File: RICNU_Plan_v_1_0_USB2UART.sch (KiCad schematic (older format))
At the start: 5 parts, among them U4 FT232RL

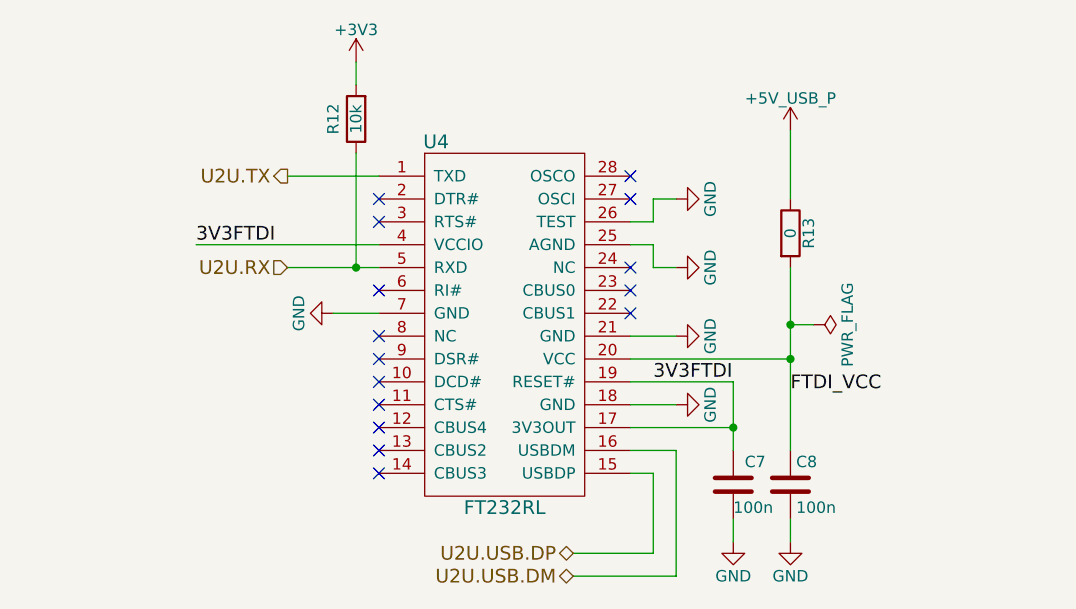
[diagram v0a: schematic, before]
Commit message: Added connections to monitor power, changed CANSTB MCU pin, moved LED pins around
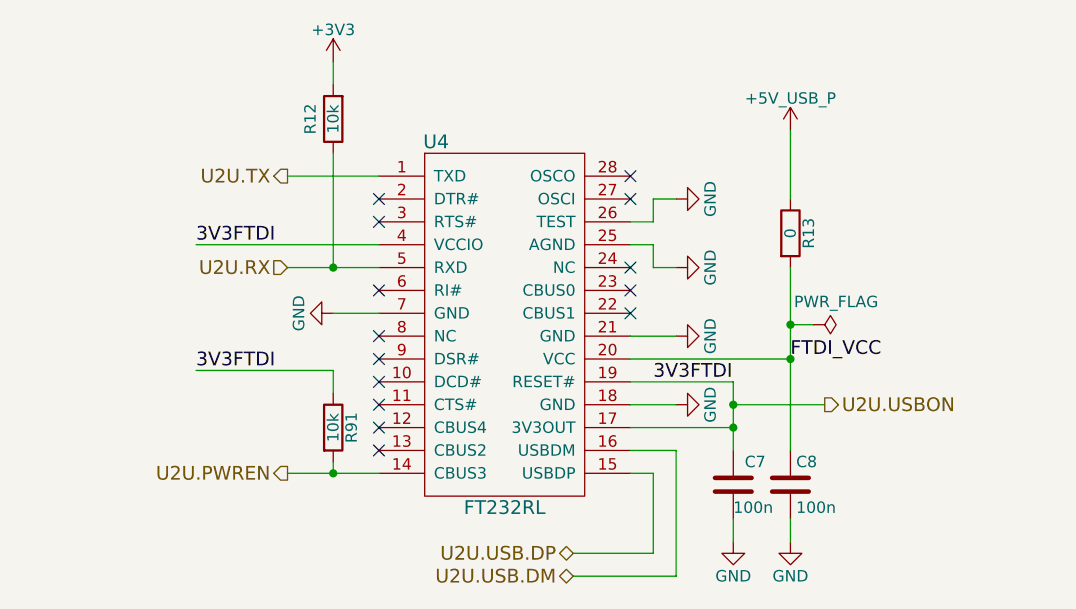
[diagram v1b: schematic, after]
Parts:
- added R91: 10k, Resistors_SMD:R_0402_NoSilk, symbol R
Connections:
- net U2U.PWREN: now reaches U4.14 (CBUS3)
- net U2U.PWREN: now also R91.2
- net 3V3FTDI renamed U2U.USBON
- net U2U.USBON: now also R91.1
- no-connect marks 15 -> 14
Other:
- moved on the sheet: R12
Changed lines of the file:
@@
 L R R12
 U 1 1 59FB130B
-P 5250 3100
-F 0 "R12" V 5350 3100 50  0000 C CNN
-F 1 "10k" V 5250 3100 50  0000 C CNN
-F 2 "Resistors_SMD:R_0402_NoSilk" V 5180 3100 50  0001 C CNN
-F 3 "" H 5250 3100 50  0001 C CNN
-	1    5250 3100
+P 5150 3100
+F 0 "R12" V 5250 3100 50  0000 C CNN
+F 1 "10k" V 5150 3100 50  0000 C CNN
+F 2 "Resistors_SMD:R_0402_NoSilk" V 5080 3100 50  0001 C CNN
+F 3 "" H 5150 3100 50  0001 C CNN
+	1    5150 3100
 	-1   0    0    1
 $EndComp
@@
 NoConn ~ 5350 4450
 NoConn ~ 5350 4550
-NoConn ~ 5350 4650
 NoConn ~ 6450 3850
 NoConn ~ 6450 3950
@@
 L +3V3 #PWR025
 U 1 1 59FB95AB
-P 5250 2850
-F 0 "#PWR025" H 5250 2700 50  0001 C CNN
-F 1 "+3V3" H 5250 2990 50  0000 C CNN
-F 2 "" H 5250 2850 50  0001 C CNN
-F 3 "" H 5250 2850 50  0001 C CNN
-	1    5250 2850
+P 5150 2850
+F 0 "#PWR025" H 5150 2700 50  0001 C CNN
+F 1 "+3V3" H 5150 2990 50  0000 C CNN
+F 2 "" H 5150 2850 50  0001 C CNN
+F 3 "" H 5150 2850 50  0001 C CNN
+	1    5150 2850
 	1    0    0    -1
 $EndComp
@@
 	6450 4650 6550 4650
 Wire Wire Line
-	6450 4450 6900 4450
-Wire Wire Line
-	6450 4150 7150 4150
+	6900 4450 6450 4450
+Wire Wire Line
+	7150 4150 6450 4150
 Wire Wire Line
 	7150 3750 7150 4550
@@
 	4950 3750 5350 3750
 Wire Wire Line
-	5250 3750 5250 3250
-Wire Wire Line
-	5250 2850 5250 2950
-Connection ~ 5250 3750
+	5150 3750 5150 3250
+Wire Wire Line
+	5150 2850 5150 2950
+Connection ~ 5150 3750
 Wire Wire Line
 	4950 3350 5350 3350
@@
 P 7250 4000
 F 0 "#FLG032" H 7250 4075 50  0001 C CNN
-F 1 "PWR_FLAG" H 7250 4150 50  0000 C CNN
+F 1 "PWR_FLAG" V 7150 4100 50  0000 C CNN
 F 2 "" H 7250 4000 50  0001 C CNN
 F 3 "" H 7250 4000 50  0001 C CNN
@@
 	7250 4000 7150 4000
 Connection ~ 7150 4000
-Text Label 7150 4300 0    60   ~ 0
+Text Label 7150 4150 0    60   ~ 0
 FTDI_VCC
+$Comp
+L R R91
+U 1 1 5A20B32A
+P 5150 4450
+F 0 "R91" V 5230 4450 50  0000 C CNN
+F 1 "10k" V 5150 4450 50  0000 C CNN
+F 2 "Resistors_SMD:R_0402_NoSilk" V 5080 4450 50  0001 C CNN
+F 3 "" H 5150 4450 50  0001 C CNN
+	1    5150 4450
+	1    0    0    -1
+$EndComp
+Wire Wire Line
+	4950 4650 5350 4650
+Wire Wire Line
+	5150 4650 5150 4600
+Wire Wire Line
+	5150 4200 5150 4300
+Connection ~ 5150 4650
+Text HLabel 4950 4650 0    60   Output ~ 0
+U2U.PWREN
+Text HLabel 7300 4350 2    60   Output ~ 0
+U2U.USBON
+Wire Wire Line
+	6900 4350 7300 4350
+Connection ~ 6900 4350
+Wire Wire Line
+	5150 4200 4550 4200
+Text Label 4550 4200 0    60   ~ 0
+3V3FTDI
 $EndSCHEMATC

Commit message: Various small changes like comment removal
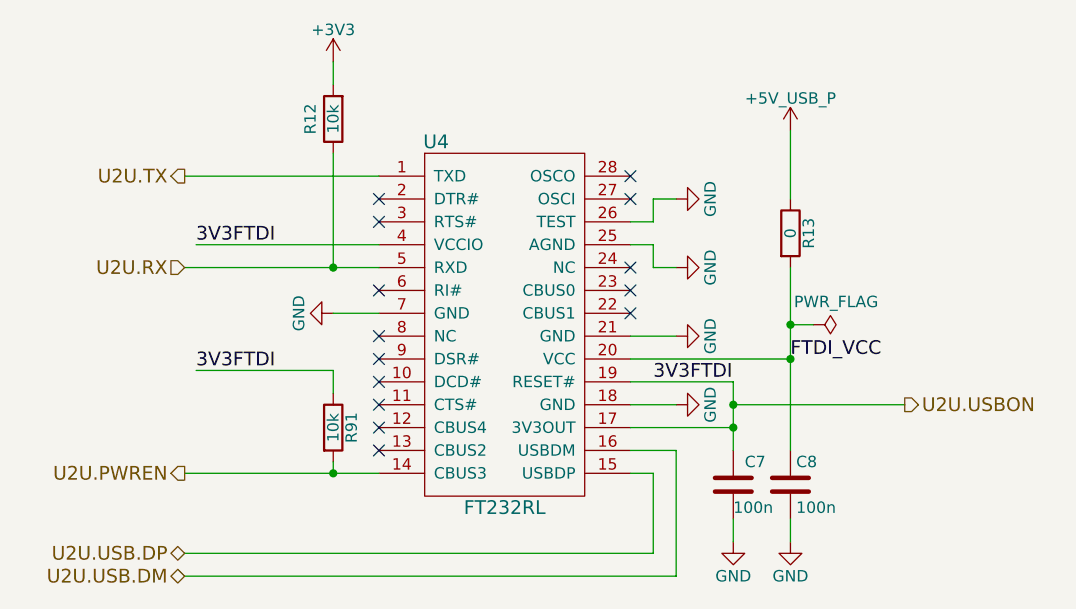
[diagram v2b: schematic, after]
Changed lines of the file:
@@
 	1    0    0    -1
 $EndComp
-Text HLabel 4950 3350 0    60   Output ~ 0
+Text HLabel 4500 3350 0    60   Output ~ 0
 U2U.TX
-Text HLabel 4950 3750 0    60   Input ~ 0
+Text HLabel 4500 3750 0    60   Input ~ 0
 U2U.RX
-Text HLabel 6200 5000 0    60   BiDi ~ 0
+Text HLabel 4500 5000 0    60   BiDi ~ 0
 U2U.USB.DP
-Text HLabel 6200 5100 0    60   BiDi ~ 0
+Text HLabel 4500 5100 0    60   BiDi ~ 0
 U2U.USB.DM
 $Comp
@@
 	7150 4150 6450 4150
 Wire Wire Line
-	7150 3750 7150 4550
+	7150 3750 7150 4000
+Wire Wire Line
+	7150 4000 7150 4150
+Wire Wire Line
+	7150 4150 7150 4550
 Wire Wire Line
 	7150 3150 7150 3450
 Connection ~ 7150 4150
 Wire Wire Line
-	4950 3750 5350 3750
+	4500 3750 5150 3750
+Wire Wire Line
+	5150 3750 5350 3750
 Wire Wire Line
 	5150 3750 5150 3250
@@
 Connection ~ 5150 3750
 Wire Wire Line
-	4950 3350 5350 3350
+	4500 3350 5350 3350
 Wire Wire Line
 	6900 4850 6900 4950
 Wire Wire Line
-	6900 4250 6900 4550
+	6900 4250 6900 4350
+Wire Wire Line
+	6900 4350 6900 4450
+Wire Wire Line
+	6900 4450 6900 4550
 Wire Wire Line
 	6450 4250 6900 4250
@@
 	6650 4050 6450 4050
 Wire Wire Line
-	6200 5000 6550 5000
+	4500 5000 6550 5000
 Wire Wire Line
 	6550 5000 6550 4650
 Wire Wire Line
-	6650 5100 6200 5100
+	6650 5100 4500 5100
 Wire Wire Line
 	5350 3950 5150 3950
@@
 $EndComp
 Wire Wire Line
-	4950 4650 5350 4650
+	4500 4650 5150 4650
+Wire Wire Line
+	5150 4650 5350 4650
 Wire Wire Line
 	5150 4650 5150 4600
@@
 	5150 4200 5150 4300
 Connection ~ 5150 4650
-Text HLabel 4950 4650 0    60   Output ~ 0
+Text HLabel 4500 4650 0    60   Output ~ 0
 U2U.PWREN
-Text HLabel 7300 4350 2    60   Output ~ 0
+Text HLabel 7650 4350 2    60   Output ~ 0
 U2U.USBON
 Wire Wire Line
-	6900 4350 7300 4350
+	6900 4350 7650 4350
 Connection ~ 6900 4350
 Wire Wire Line

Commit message: Deleting PDFs
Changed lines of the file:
@@
 	7150 4150 6450 4150
 Wire Wire Line
-	7150 3750 7150 4000
-Wire Wire Line
-	7150 4000 7150 4150
-Wire Wire Line
-	7150 4150 7150 4550
+	7150 3750 7150 4550
 Wire Wire Line
 	7150 3150 7150 3450
 Connection ~ 7150 4150
 Wire Wire Line
-	4500 3750 5150 3750
-Wire Wire Line
-	5150 3750 5350 3750
+	4500 3750 5350 3750
 Wire Wire Line
 	5150 3750 5150 3250
@@
 	6900 4850 6900 4950
 Wire Wire Line
-	6900 4250 6900 4350
-Wire Wire Line
-	6900 4350 6900 4450
-Wire Wire Line
-	6900 4450 6900 4550
+	6900 4250 6900 4550
 Wire Wire Line
 	6450 4250 6900 4250
@@
 $EndComp
 Wire Wire Line
-	4500 4650 5150 4650
-Wire Wire Line
-	5150 4650 5350 4650
+	4500 4650 5350 4650
 Wire Wire Line
 	5150 4650 5150 4600
